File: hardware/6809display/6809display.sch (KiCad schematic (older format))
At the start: 36 parts, among them J1 Video Out, J2 To Computer, Q1 BC557, Q2 BC557, Q3 BC557, U1 74HC04, U2 74HC04, U3 74HC393, U4 SAA5020, U5 SAA5050, U6 IDT7132, U7 74HC08, Y1 Crystal

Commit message: ide comtroller
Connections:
- net VCC: no longer U1.11, U1.13
- net ~Slot-Select: now also U1.11; no longer U7.1
- net at U1.10: now also U7.1
- net at U1.12: now also U6.1 (/CEL)
- net at U7.3: now also U1.13; no longer U6.1 (/CEL)
- no-connect marks 40 -> 38
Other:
- moved on the sheet: U1E, U1F, U7A
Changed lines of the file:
@@
 NoConn ~ 5450 6700
 NoConn ~ 5450 7050
-NoConn ~ 5450 7750
-NoConn ~ 5450 7400
 $Comp
 L 74xx:74HC04 U1
 U 6 1 606F7EB3
-P 5150 7750
-F 0 "U1" H 5100 7800 50  0000 C CNN
-F 1 "74HC04" H 5100 7700 50  0000 C CNN
-F 2 "" H 5150 7750 50  0001 C CNN
-F 3 "https://assets.nexperia.com/documents/data-sheet/74HC_HCT04.pdf" H 5150 7750 50  0001 C CNN
-	6    5150 7750
+P 7250 5850
+F 0 "U1" H 7200 5900 50  0000 C CNN
+F 1 "74HC04" H 7200 5800 50  0000 C CNN
+F 2 "" H 7250 5850 50  0001 C CNN
+F 3 "https://assets.nexperia.com/documents/data-sheet/74HC_HCT04.pdf" H 7250 5850 50  0001 C CNN
+	6    7250 5850
 	1    0    0    -1
 $EndComp
@@
 L 74xx:74HC04 U1
 U 5 1 606F65D4
-P 5150 7400
-F 0 "U1" H 5100 7450 50  0000 C CNN
-F 1 "74HC04" H 5100 7350 50  0000 C CNN
-F 2 "" H 5150 7400 50  0001 C CNN
-F 3 "https://assets.nexperia.com/documents/data-sheet/74HC_HCT04.pdf" H 5150 7400 50  0001 C CNN
-	5    5150 7400
+P 6050 5750
+F 0 "U1" H 6000 5800 50  0000 C CNN
+F 1 "74HC04" H 6000 5700 50  0000 C CNN
+F 2 "" H 6050 5750 50  0001 C CNN
+F 3 "https://assets.nexperia.com/documents/data-sheet/74HC_HCT04.pdf" H 6050 5750 50  0001 C CNN
+	5    6050 5750
 	1    0    0    -1
 $EndComp
 Wire Wire Line
 	4850 6700 4850 7050
-Wire Wire Line
-	4850 7400 4850 7750
 Entry Wire Line
 	10750 1400 10850 1500
@@
 Text GLabel 7650 6150 0    50   Input ~ 0
 ~Read-Enable
-Text GLabel 6950 5750 0    50   Input ~ 0
+Text GLabel 5750 5750 0    50   Input ~ 0
 ~Slot-Select
 Entry Wire Line
-	6750 5950 6650 6050
-Text Label 6950 5950 2    50   ~ 0
+	6150 5950 6050 6050
+Text Label 6350 5950 2    50   ~ 0
 CA11
 Wire Wire Line
-	6950 5950 6750 5950
+	6350 5950 6150 5950
 Text Notes 8100 5300 0    50   ~ 0
 Teletext RAM\nText Page 1: E800-EBFF\nText Page 2: EC00-EFFF\n
@@
 L 74xx:74LS08 U7
 U 1 1 6101C4B8
-P 7250 5850
-F 0 "U7" H 7250 5900 50  0000 C CNN
-F 1 "74HC08" H 7250 5800 50  0000 C CNN
-F 2 "" H 7250 5850 50  0001 C CNN
-F 3 "http://www.ti.com/lit/gpn/sn74LS08" H 7250 5850 50  0001 C CNN
-	1    7250 5850
+P 6650 5850
+F 0 "U7" H 6650 5900 50  0000 C CNN
+F 1 "74HC08" H 6650 5800 50  0000 C CNN
+F 2 "" H 6650 5850 50  0001 C CNN
+F 3 "http://www.ti.com/lit/gpn/sn74LS08" H 6650 5850 50  0001 C CNN
+	1    6650 5850
 	1    0    0    -1
 $EndComp
@@
 	1    0    0    -1
 $EndComp
-Text GLabel 4850 7400 0    50   Input ~ 0
-+5v
 Wire Wire Line
 	7650 8250 7450 8250
@@
 Wire Wire Line
 	8950 4100 9050 4100
+$Comp
+L power:PWR_FLAG #FLG0101
+U 1 1 61A719D1
+P 9050 4100
+F 0 "#FLG0101" H 9050 4175 50  0001 C CNN
+F 1 "PWR_FLAG" H 9050 4273 50  0001 C CNN
+F 2 "" H 9050 4100 50  0001 C CNN
+F 3 "~" H 9050 4100 50  0001 C CNN
+	1    9050 4100
+	1    0    0    -1
+$EndComp
+Connection ~ 9050 4100
+Wire Wire Line
+	9050 4100 9150 4100
 Wire Bus Line
-	6650 6000 6650 6100
+	6050 6000 6050 6100
 Wire Bus Line
 	3600 2750 3600 3150
@@
 Wire Bus Line
 	10850 1500 10850 3500
-$Comp
-L power:PWR_FLAG #FLG0101
-U 1 1 61A719D1
-P 9050 4100
-F 0 "#FLG0101" H 9050 4175 50  0001 C CNN
-F 1 "PWR_FLAG" H 9050 4273 50  0001 C CNN
-F 2 "" H 9050 4100 50  0001 C CNN
-F 3 "~" H 9050 4100 50  0001 C CNN
-	1    9050 4100
-	1    0    0    -1
-$EndComp
-Connection ~ 9050 4100
-Wire Wire Line
-	9050 4100 9150 4100
 $EndSCHEMATC

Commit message: text card
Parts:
- added C10, C7, C8, C9: 0.1uF, Capacitor_THT:C_Disc_D5.0mm_W2.5mm_P5.00mm, symbol Device:C
- added NT1: Net-Tie_2, NetTie:NetTie-2_SMD_Pad0.5mm, symbol Device:Net-Tie_2
- added U10, U8, U9: 74HC283, Package_DIP:DIP-16_W7.62mm_LongPads, symbol 74xx:74LS283
- C1, C2, C3, C4, C5, C6: footprint (none) -> Capacitor_THT:C_Disc_D5.0mm_W2.5mm_P5.00mm
- J1: footprint (none) -> Connector_PinHeader_2.54mm:PinHeader_1x05_P2.54mm_Vertical
- J2: footprint SS-50_SS-50_BOARD_CONNECTOR -> Connector_PinHeader_2.54mm:PinHeader_2x25_P2.54mm_Vertical
- R1, R10, R11, R12, R13, R14, R15, R16, R17, R2, R3, R4, R5, R6, R7, R8, R9: footprint (none) -> Resistor_THT:R_Axial_DIN0309_L9.0mm_D3.2mm_P12.70mm_Horizontal
- U1, U2, U3, U7: footprint (none) -> Package_DIP:DIP-14_W7.62mm_LongPads
- U4: footprint (none) -> Package_DIP:DIP-24_W15.24mm_LongPads
- U5: footprint (none) -> Package_DIP:DIP-28_W15.24mm_LongPads
- U6: footprint (none) -> Package_DIP:DIP-48_W15.24mm_LongPads
- Y1: value Crystal -> 6MHz; footprint (none) -> Crystal:Resonator-2Pin_W7.0mm_H2.5mm
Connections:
- net A3: now also U10.1 (S2); no longer U3.13 (CP), U3.6 (Q3)
- net A4: now also U10.13 (S3); no longer U3.11 (Q0)
- net A5: now also U10.10 (S4); no longer U3.10 (Q1)
- net A6: now also U9.4 (S1); no longer U4.19 (A0)
- net A7: now also U9.1 (S2); no longer U4.20 (A1)
- net A8: now also U9.13 (S3); no longer U4.21 (A2)
- net A9: now also U9.10 (S4); no longer U4.22 (A3)
- net GND: now also C1.1, C2.1, C3.1, C5.1, U6.44 (A10R), C10.1, C7.1, C8.1, C9.1, NT1.1, U10.5 (A1), U10.8 (GND), U8.12 (A4), U8.7 (C0), U8.8 (GND), U9.12 (A4), U9.14 (A3), U9.3 (A2), U9.5 (A1), U9.8 (GND); no longer C1.2, C2.2, C3.2, C5.2, U5.2 (~SI)
- net VCC: now also C1.2, C2.2, C3.2, C5.2, C10.2, C7.2, C8.2, C9.2, U10.16 (VCC), U8.16 (VCC), U9.16 (VCC); no longer C1.1, C2.1, C3.1, C5.1
- net A10 renamed SA4
- net SA4: now also U10.6 (B1), U8.14 (A3); no longer U6.44 (A10R)
- new net: U10.3 (A2), U3.13 (CP), U3.6 (Q3)
- new net: U10.12 (A4), U3.10 (Q1)
- new net: U10.14 (A3), U3.11 (Q0)
- new net: NT1.2, U5.2 (~SI)
- new net: U10.11 (B4), U8.4 (S1)
- new net: U10.4 (S1), U9.11 (B4)
- new net: U10.7 (C0), U8.9 (C4)
- new net: U10.9 (C4), U9.7 (C0)
- new net: U8.1 (S2), U9.6 (B1)
- new net: U8.10 (S4), U9.15 (B3)
- new net: U8.13 (S3), U9.2 (B2)
- new net SA0: U10.2 (B2), U4.19 (A0), U8.6 (B1)
- new net SA1: U10.15 (B3), U4.20 (A1), U8.2 (B2)
- new net SA2: U4.21 (A2), U8.15 (B3), U8.5 (A1)
- new net SA3: U4.22 (A3), U8.11 (B4), U8.3 (A2)
- no-connect marks 38 -> 39
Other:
- moved on the sheet: C1, C2, C3, C4, C5, C6, J2, U1E, U1F, U1G, U2D, U2E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

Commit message: clock and more
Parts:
- removed NT1: Net-Tie_2, NetTie:NetTie-2_SMD_Pad0.5mm, symbol Device:Net-Tie_2
- R16, R17: footprint Resistor_THT:R_Axial_DIN0309_L9.0mm_D3.2mm_P12.70mm_Horizontal -> Resistor_THT:R_Axial_DIN0207_L6.3mm_D2.5mm_P7.62mm_Horizontal
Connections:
- net GND: now also U5.2 (~SI)
- net at U1.4, U4.2 (F6), Y1.2: now also R17.1; no longer R17.2
- net at R16.2, U1.2, U1.3: now also R17.2; no longer R17.1
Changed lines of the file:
@@
 F 0 "R16" V 900 1550 50  0000 C CNN
 F 1 "2k2" V 700 1550 50  0000 C CNN
-F 2 "Resistor_THT:R_Axial_DIN0309_L9.0mm_D3.2mm_P12.70mm_Horizontal" H 800 1550 50  0001 C CNN
+F 2 "Resistor_THT:R_Axial_DIN0207_L6.3mm_D2.5mm_P7.62mm_Horizontal" H 800 1550 50  0001 C CNN
 F 3 "~" H 800 1550 50  0001 C CNN
 	1    800  1550
@@
 F 0 "R17" V 1900 1550 50  0000 C CNN
 F 1 "2k2" V 1700 1550 50  0000 C CNN
-F 2 "Resistor_THT:R_Axial_DIN0309_L9.0mm_D3.2mm_P12.70mm_Horizontal" H 1800 1550 50  0001 C CNN
+F 2 "Resistor_THT:R_Axial_DIN0207_L6.3mm_D2.5mm_P7.62mm_Horizontal" H 1800 1550 50  0001 C CNN
 F 3 "~" H 1800 1550 50  0001 C CNN
 	1    1800 1550
-	0    -1   -1   0
+	0    1    -1   0
 $EndComp
 Wire Wire Line
@@
 Wire Wire Line
 	3950 2450 3950 2550
-Text GLabel 3750 2700 0    50   Input ~ 0
+Text GLabel 3950 2700 0    50   Input ~ 0
 GND
 Text GLabel 4600 3850 3    50   Input ~ 0
@@
 Text GLabel 3950 2800 0    50   Input ~ 0
 GND
-$Comp
-L Device:Net-Tie_2 NT1
-U 1 1 610191AE
-P 3850 2700
-F 0 "NT1" H 3850 2881 50  0001 C CNN
-F 1 "Net-Tie_2" H 3850 2790 50  0001 C CNN
-F 2 "NetTie:NetTie-2_SMD_Pad0.5mm" H 3850 2700 50  0001 C CNN
-F 3 "~" H 3850 2700 50  0001 C CNN
-	1    3850 2700
-	1    0    0    -1
-$EndComp
 Connection ~ 3250 10550
 Connection ~ 3250 10850

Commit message: digital logic wired up
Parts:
- R1, R10, R11, R12, R13, R14, R15, R2, R3, R4, R5, R6, R7, R8, R9: footprint Resistor_THT:R_Axial_DIN0309_L9.0mm_D3.2mm_P12.70mm_Horizontal -> Resistor_THT:R_Axial_DIN0207_L6.3mm_D2.5mm_P7.62mm_Horizontal
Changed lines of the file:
@@
 F 0 "R14" V 6045 3600 50  0000 C CNN
 F 1 "470" V 6136 3600 50  0000 C CNN
-F 2 "Resistor_THT:R_Axial_DIN0309_L9.0mm_D3.2mm_P12.70mm_Horizontal" H 6250 3600 50  0001 C CNN
+F 2 "Resistor_THT:R_Axial_DIN0207_L6.3mm_D2.5mm_P7.62mm_Horizontal" H 6250 3600 50  0001 C CNN
 F 3 "~" H 6250 3600 50  0001 C CNN
 	1    6250 3600
@@
 F 0 "R15" H 7118 3546 50  0000 L CNN
 F 1 "82" H 7118 3455 50  0000 L CNN
-F 2 "Resistor_THT:R_Axial_DIN0309_L9.0mm_D3.2mm_P12.70mm_Horizontal" H 7050 3500 50  0001 C CNN
+F 2 "Resistor_THT:R_Axial_DIN0207_L6.3mm_D2.5mm_P7.62mm_Horizontal" H 7050 3500 50  0001 C CNN
 F 3 "~" H 7050 3500 50  0001 C CNN
 	1    7050 3500
@@
 F 0 "R13" H 6450 3950 50  0000 L CNN
 F 1 "100" H 6450 3850 50  0000 L CNN
-F 2 "Resistor_THT:R_Axial_DIN0309_L9.0mm_D3.2mm_P12.70mm_Horizontal" H 6650 3900 50  0001 C CNN
+F 2 "Resistor_THT:R_Axial_DIN0207_L6.3mm_D2.5mm_P7.62mm_Horizontal" H 6650 3900 50  0001 C CNN
 F 3 "~" H 6650 3900 50  0001 C CNN
 	1    6650 3900
@@
 F 0 "R11" H 5400 3750 50  0000 L CNN
 F 1 "1k" H 5400 3650 50  0000 L CNN
-F 2 "Resistor_THT:R_Axial_DIN0309_L9.0mm_D3.2mm_P12.70mm_Horizontal" H 5550 3700 50  0001 C CNN
+F 2 "Resistor_THT:R_Axial_DIN0207_L6.3mm_D2.5mm_P7.62mm_Horizontal" H 5550 3700 50  0001 C CNN
 F 3 "~" H 5550 3700 50  0001 C CNN
 	1    5550 3700
@@
 F 0 "R12" H 6150 3950 50  0000 L CNN
 F 1 "470" H 6150 3850 50  0000 L CNN
-F 2 "Resistor_THT:R_Axial_DIN0309_L9.0mm_D3.2mm_P12.70mm_Horizontal" H 6350 3900 50  0001 C CNN
+F 2 "Resistor_THT:R_Axial_DIN0207_L6.3mm_D2.5mm_P7.62mm_Horizontal" H 6350 3900 50  0001 C CNN
 F 3 "~" H 6350 3900 50  0001 C CNN
 	1    6350 3900
@@
 F 0 "R9" V 6045 2850 50  0000 C CNN
 F 1 "470" V 6136 2850 50  0000 C CNN
-F 2 "Resistor_THT:R_Axial_DIN0309_L9.0mm_D3.2mm_P12.70mm_Horizontal" H 6250 2850 50  0001 C CNN
+F 2 "Resistor_THT:R_Axial_DIN0207_L6.3mm_D2.5mm_P7.62mm_Horizontal" H 6250 2850 50  0001 C CNN
 F 3 "~" H 6250 2850 50  0001 C CNN
 	1    6250 2850
@@
 F 0 "R10" H 7118 2796 50  0000 L CNN
 F 1 "82" H 7118 2705 50  0000 L CNN
-F 2 "Resistor_THT:R_Axial_DIN0309_L9.0mm_D3.2mm_P12.70mm_Horizontal" H 7050 2750 50  0001 C CNN
+F 2 "Resistor_THT:R_Axial_DIN0207_L6.3mm_D2.5mm_P7.62mm_Horizontal" H 7050 2750 50  0001 C CNN
 F 3 "~" H 7050 2750 50  0001 C CNN
 	1    7050 2750
@@
 F 0 "R8" H 6450 3200 50  0000 L CNN
 F 1 "100" H 6450 3100 50  0000 L CNN
-F 2 "Resistor_THT:R_Axial_DIN0309_L9.0mm_D3.2mm_P12.70mm_Horizontal" H 6650 3150 50  0001 C CNN
+F 2 "Resistor_THT:R_Axial_DIN0207_L6.3mm_D2.5mm_P7.62mm_Horizontal" H 6650 3150 50  0001 C CNN
 F 3 "~" H 6650 3150 50  0001 C CNN
 	1    6650 3150
@@
 F 0 "R6" H 5400 3000 50  0000 L CNN
 F 1 "1k" H 5400 2900 50  0000 L CNN
-F 2 "Resistor_THT:R_Axial_DIN0309_L9.0mm_D3.2mm_P12.70mm_Horizontal" H 5550 2950 50  0001 C CNN
+F 2 "Resistor_THT:R_Axial_DIN0207_L6.3mm_D2.5mm_P7.62mm_Horizontal" H 5550 2950 50  0001 C CNN
 F 3 "~" H 5550 2950 50  0001 C CNN
 	1    5550 2950
@@
 F 0 "R7" H 6150 3200 50  0000 L CNN
 F 1 "470" H 6150 3100 50  0000 L CNN
-F 2 "Resistor_THT:R_Axial_DIN0309_L9.0mm_D3.2mm_P12.70mm_Horizontal" H 6350 3150 50  0001 C CNN
+F 2 "Resistor_THT:R_Axial_DIN0207_L6.3mm_D2.5mm_P7.62mm_Horizontal" H 6350 3150 50  0001 C CNN
 F 3 "~" H 6350 3150 50  0001 C CNN
 	1    6350 3150
@@
 F 0 "R4" V 6045 2100 50  0000 C CNN
 F 1 "470" V 6136 2100 50  0000 C CNN
-F 2 "Resistor_THT:R_Axial_DIN0309_L9.0mm_D3.2mm_P12.70mm_Horizontal" H 6250 2100 50  0001 C CNN
+F 2 "Resistor_THT:R_Axial_DIN0207_L6.3mm_D2.5mm_P7.62mm_Horizontal" H 6250 2100 50  0001 C CNN
 F 3 "~" H 6250 2100 50  0001 C CNN
 	1    6250 2100
@@
 F 0 "R5" H 7118 2046 50  0000 L CNN
 F 1 "82" H 7118 1955 50  0000 L CNN
-F 2 "Resistor_THT:R_Axial_DIN0309_L9.0mm_D3.2mm_P12.70mm_Horizontal" H 7050 2000 50  0001 C CNN
+F 2 "Resistor_THT:R_Axial_DIN0207_L6.3mm_D2.5mm_P7.62mm_Horizontal" H 7050 2000 50  0001 C CNN
 F 3 "~" H 7050 2000 50  0001 C CNN
 	1    7050 2000
@@
 F 0 "R3" H 6450 2450 50  0000 L CNN
 F 1 "100" H 6450 2350 50  0000 L CNN
-F 2 "Resistor_THT:R_Axial_DIN0309_L9.0mm_D3.2mm_P12.70mm_Horizontal" H 6650 2400 50  0001 C CNN
+F 2 "Resistor_THT:R_Axial_DIN0207_L6.3mm_D2.5mm_P7.62mm_Horizontal" H 6650 2400 50  0001 C CNN
 F 3 "~" H 6650 2400 50  0001 C CNN
 	1    6650 2400
@@
 F 0 "R1" H 5400 2250 50  0000 L CNN
 F 1 "1k" H 5400 2150 50  0000 L CNN
-F 2 "Resistor_THT:R_Axial_DIN0309_L9.0mm_D3.2mm_P12.70mm_Horizontal" H 5550 2200 50  0001 C CNN
+F 2 "Resistor_THT:R_Axial_DIN0207_L6.3mm_D2.5mm_P7.62mm_Horizontal" H 5550 2200 50  0001 C CNN
 F 3 "~" H 5550 2200 50  0001 C CNN
 	1    5550 2200
@@
 F 0 "R2" H 6150 2450 50  0000 L CNN
 F 1 "470" H 6150 2350 50  0000 L CNN
-F 2 "Resistor_THT:R_Axial_DIN0309_L9.0mm_D3.2mm_P12.70mm_Horizontal" H 6350 2400 50  0001 C CNN
+F 2 "Resistor_THT:R_Axial_DIN0207_L6.3mm_D2.5mm_P7.62mm_Horizontal" H 6350 2400 50  0001 C CNN
 F 3 "~" H 6350 2400 50  0001 C CNN
 	1    6350 2400

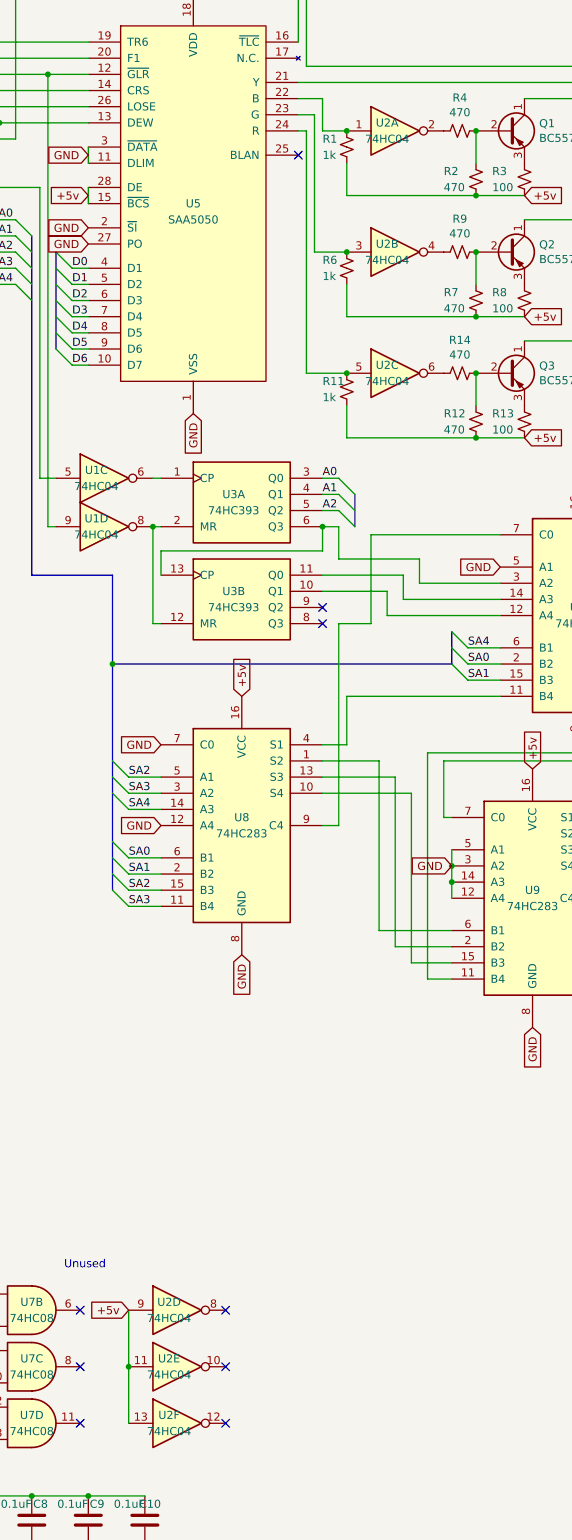
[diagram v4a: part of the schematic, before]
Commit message: has a placement overlap
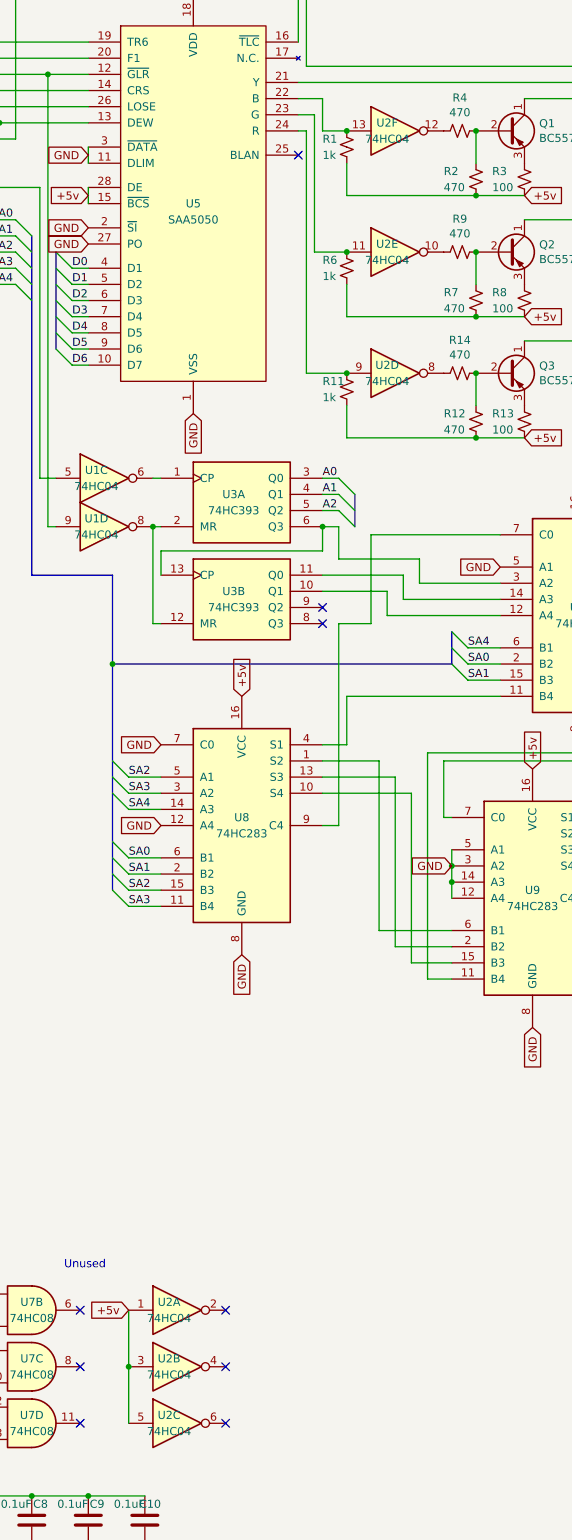
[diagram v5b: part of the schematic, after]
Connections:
- net VCC: now also U2.1, U2.3, U2.5; no longer U2.11, U2.13, U2.9
- net at R1.1, U5.22 (B): now also U2.13; no longer U2.1
- net at R6.1, U5.23 (G): now also U2.11; no longer U2.3
- net at R11.1, U5.24 (R): now also U2.9; no longer U2.5
- net at R4.2: now also U2.12; no longer U2.2
- net at R9.2: now also U2.10; no longer U2.4
- net at R14.2: now also U2.8; no longer U2.6
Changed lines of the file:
@@
 $Comp
 L 74xx:74HC04 U2
-U 5 1 606E72FD
+U 2 1 606E72FD
 P 4500 9750
 F 0 "U2" H 4450 9800 50  0000 C CNN
@@
 F 2 "Package_DIP:DIP-14_W7.62mm_LongPads" H 4500 9750 50  0001 C CNN
 F 3 "https://assets.nexperia.com/documents/data-sheet/74HC_HCT04.pdf" H 4500 9750 50  0001 C CNN
-	5    4500 9750
+	2    4500 9750
 	1    0    0    -1
 $EndComp
 $Comp
 L 74xx:74HC04 U2
-U 6 1 606E899D
+U 3 1 606E899D
 P 4500 10100
 F 0 "U2" H 4450 10150 50  0000 C CNN
@@
 F 2 "Package_DIP:DIP-14_W7.62mm_LongPads" H 4500 10100 50  0001 C CNN
 F 3 "https://assets.nexperia.com/documents/data-sheet/74HC_HCT04.pdf" H 4500 10100 50  0001 C CNN
-	6    4500 10100
+	3    4500 10100
 	1    0    0    -1
 $EndComp
@@
 $Comp
 L 74xx:74HC04 U2
-U 3 1 606E2126
+U 4 1 606E2126
 P 5850 3600
 F 0 "U2" H 5800 3650 50  0000 C CNN
@@
 F 2 "Package_DIP:DIP-14_W7.62mm_LongPads" H 5850 3600 50  0001 C CNN
 F 3 "https://assets.nexperia.com/documents/data-sheet/74HC_HCT04.pdf" H 5850 3600 50  0001 C CNN
-	3    5850 3600
+	4    5850 3600
 	1    0    0    -1
 $EndComp
 $Comp
 L 74xx:74HC04 U2
-U 2 1 606E11CF
+U 5 1 606E11CF
 P 5850 2850
 F 0 "U2" H 5800 2900 50  0000 C CNN
@@
 F 2 "Package_DIP:DIP-14_W7.62mm_LongPads" H 5850 2850 50  0001 C CNN
 F 3 "https://assets.nexperia.com/documents/data-sheet/74HC_HCT04.pdf" H 5850 2850 50  0001 C CNN
-	2    5850 2850
+	5    5850 2850
 	1    0    0    -1
 $EndComp
 $Comp
 L 74xx:74HC04 U2
-U 1 1 606DFD5F
+U 6 1 606DFD5F
 P 5850 2100
 F 0 "U2" H 5800 2150 50  0000 C CNN
@@
 F 2 "Package_DIP:DIP-14_W7.62mm_LongPads" H 5850 2100 50  0001 C CNN
 F 3 "https://assets.nexperia.com/documents/data-sheet/74HC_HCT04.pdf" H 5850 2100 50  0001 C CNN
-	1    5850 2100
+	6    5850 2100
 	1    0    0    -1
 $EndComp
@@
 $Comp
 L 74xx:74HC04 U2
-U 4 1 606E55BE
+U 1 1 606E55BE
 P 4500 9400
 F 0 "U2" H 4450 9450 50  0000 C CNN
@@
 F 2 "Package_DIP:DIP-14_W7.62mm_LongPads" H 4500 9400 50  0001 C CNN
 F 3 "https://assets.nexperia.com/documents/data-sheet/74HC_HCT04.pdf" H 4500 9400 50  0001 C CNN
-	4    4500 9400
-	1    0    0    -1
-$EndComp
+	1    4500 9400
+	1    0    0    -1
+$EndComp

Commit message: expansion board
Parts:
- added Logo1: Pinnated, Pinnated:Pinnule, symbol aspt:Pinnated
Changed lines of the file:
@@
 Wire Bus Line
 	15650 1150 15650 3150
+$Comp
+L aspt:Pinnated Logo1
+U 1 1 60AA09D0
+P 4950 10700
+F 0 "Logo1" H 4975 10746 50  0000 L CNN
+F 1 "Pinnated" H 4975 10655 50  0000 L CNN
+F 2 "Pinnated:Pinnule" H 4950 10700 50  0001 C CNN
+F 3 "" H 4950 10700 50  0001 C CNN
+	1    4950 10700
+	1    0    0    -1
+$EndComp
 $EndSCHEMATC

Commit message: finished and Gerbers generated
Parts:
- J2: footprint Connector_PinHeader_2.54mm:PinHeader_2x25_P2.54mm_Vertical -> Connector_IDC:IDC-Header_2x25_P2.54mm_Vertical
- Q1, Q2, Q3: footprint Package_TO_SOT_THT:TO-92_Inline -> Package_TO_SOT_THT:TO-92_Inline_Wide
- U1, U2, U3, U7: footprint Package_DIP:DIP-14_W7.62mm_LongPads -> Package_DIP:DIP-14_W7.62mm_Socket_LongPads
- U10, U8, U9: footprint Package_DIP:DIP-16_W7.62mm_LongPads -> Package_DIP:DIP-16_W7.62mm_Socket_LongPads
- U4: footprint Package_DIP:DIP-24_W15.24mm_LongPads -> Package_DIP:DIP-24_W15.24mm_Socket_LongPads
- U5: footprint Package_DIP:DIP-28_W15.24mm_LongPads -> Package_DIP:DIP-28_W15.24mm_Socket_LongPads
- U6: footprint Package_DIP:DIP-48_W15.24mm_LongPads -> Package_DIP:DIP-48_W15.24mm_Socket_LongPads
